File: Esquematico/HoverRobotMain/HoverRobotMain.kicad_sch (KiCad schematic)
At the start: 19 parts, among them J1 Screw_Terminal_01x02, J2 Ultrasonido Trasero izquierdo, J3 Ultrasonido frontal derecho, J4 Ultrasonido Frontal izquierdo, J5 Ultrasonido Trasero derecho, J6 Raspberry pi 5, J7 Motor control board, U1 ESP32-WROOM-32, U2 MPU-6050, U3 LM2576HVS-ADJ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

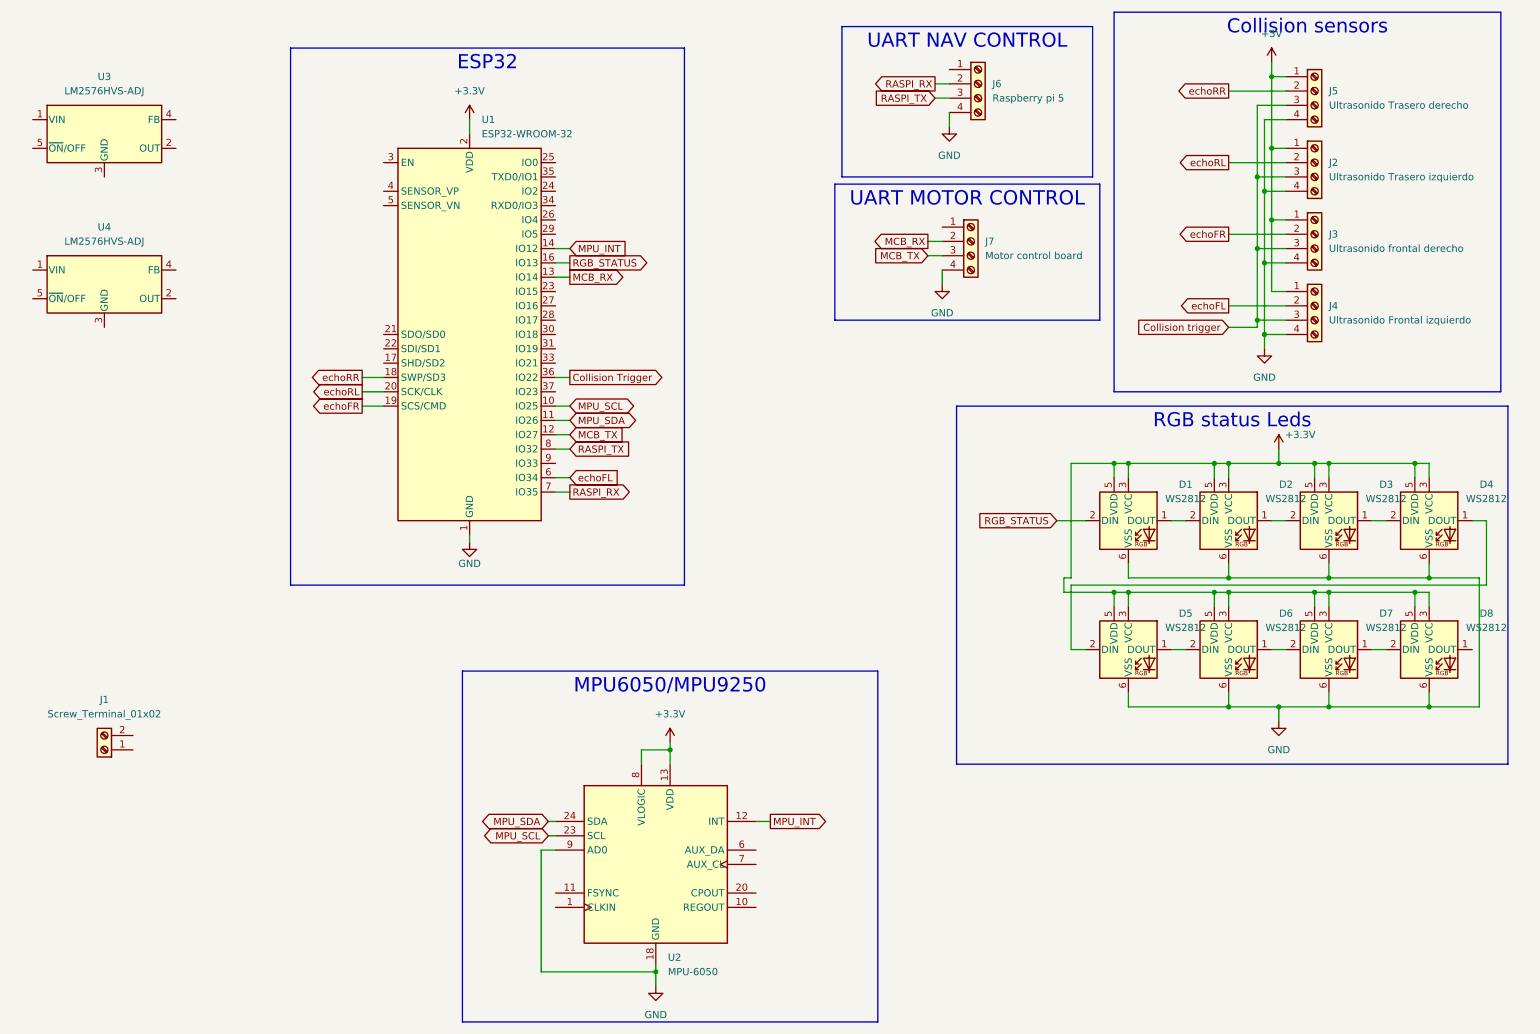
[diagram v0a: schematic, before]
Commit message: Avances en esquematico
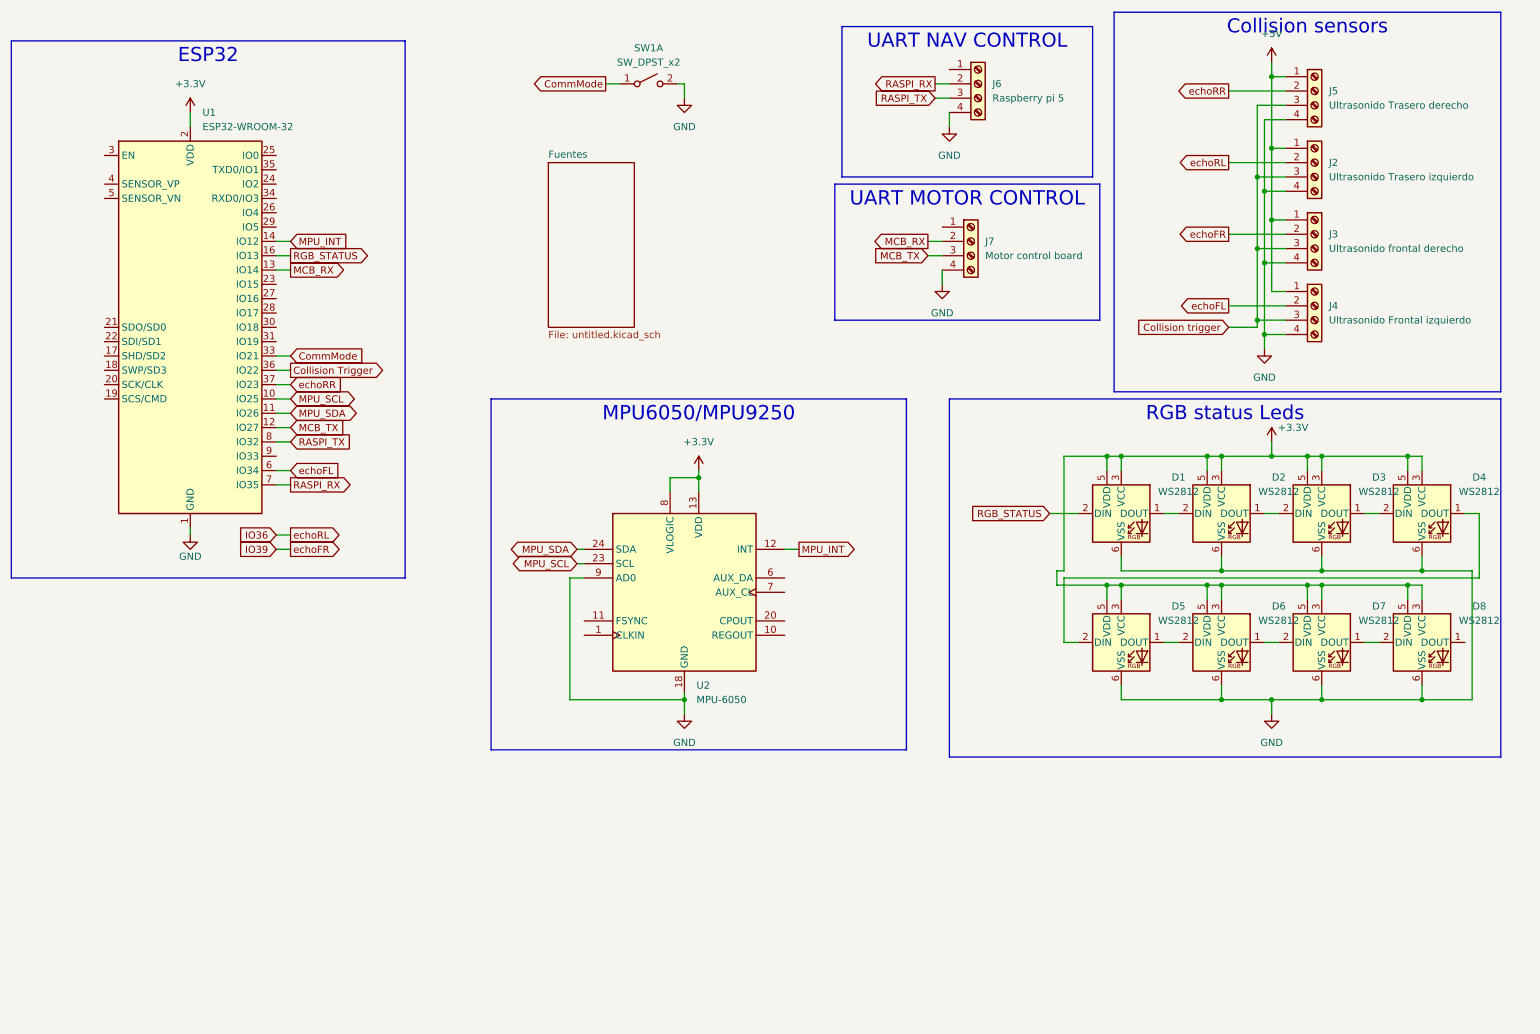
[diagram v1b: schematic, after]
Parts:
- removed J1: Screw_Terminal_01x02, symbol Connector:Screw_Terminal_01x02
- removed U3, U4: LM2576HVS-ADJ, Package_TO_SOT_SMD:TO-263-5_TabPin3, symbol Regulator_Switching:LM2576HVS-ADJ
- added SW1: SW_DPST_x2, symbol Switch:SW_DPST_x2
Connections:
- net GND: now also SW1.2 (B)
- net echoRR: now also U1.37 (IO23); no longer U1.18 (SWP/SD3)
- net CommMode: now reaches U1.33 (IO21)
- net CommMode: now also SW1.1 (A)
- net echoFR: no longer names the net of U1.19 (SCS/CMD)
- net echoFR: no longer J3.2 (Pin_2)
- net echoRL: no longer names the net of U1.20 (SCK/CLK)
- net echoRL: no longer J2.2 (Pin_2)
- new net IO36: J2.2 (Pin_2)
- new net IO39: J3.2 (Pin_2)
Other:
- added sheet Fuentes (untitled.kicad_sch)
- moved on the sheet: D1, D2, D3, D4, D5, D6, D7, D8, U1, U2
